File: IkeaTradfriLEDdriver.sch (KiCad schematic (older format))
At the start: 17 parts, among them J2 IKEA Zigbit module, J3 led strip, Q1 BUZ11, Q2 BC547, U1 LM741, U2 LM1117-3.3

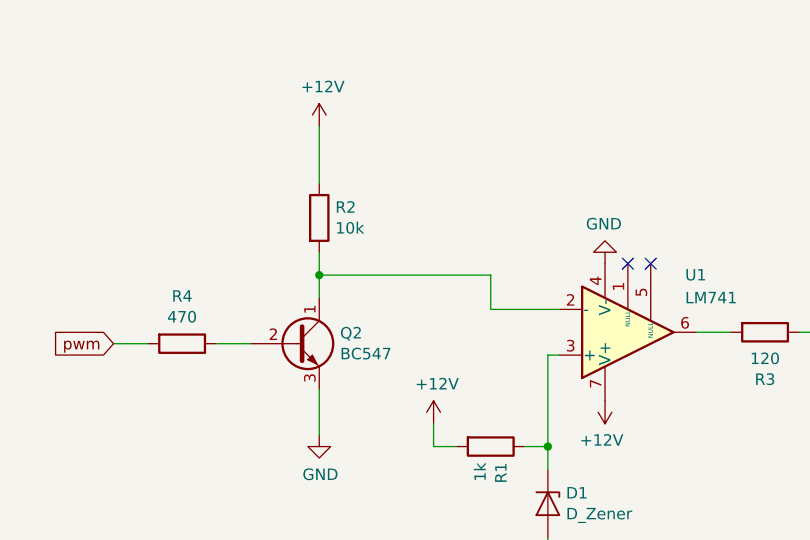
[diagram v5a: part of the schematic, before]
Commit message: Chybejici rezistor, opravene schema
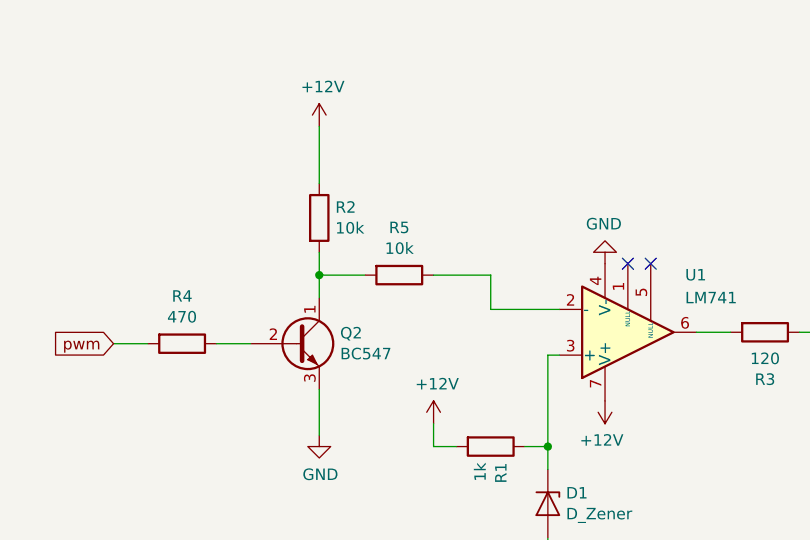
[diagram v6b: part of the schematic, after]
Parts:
- added R5: 10k, symbol Device:R
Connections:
- net at Q2.1 (C), R2.2: now also R5.2; no longer U1.2 (-)
- new net: R5.1, U1.2 (-)
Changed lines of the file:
@@
 	3250 3450 3250 3250
-Wire Wire Line
-	3250 2850 3250 2750
 Wire Wire Line
 	3250 2350 3250 2100
 Wire Wire Line
-	3250 2750 4000 2750
-Wire Wire Line
 	4000 2750 4000 2900
-Connection ~ 3250 2750
-Wire Wire Line
-	3250 2750 3250 2650
 $Comp
 L Connector:Conn_01x04_Male J3
@@
 Wire Wire Line
 	1250 2600 1250 2900
+Wire Wire Line
+	3250 2650 3250 2750
+$Comp
+L Device:R R5
+U 1 1 5C76BFEA
+P 3600 2750
+F 0 "R5" V 3393 2750 50  0000 C CNN
+F 1 "10k" V 3484 2750 50  0000 C CNN
+F 2 "" V 3530 2750 50  0001 C CNN
+F 3 "~" H 3600 2750 50  0001 C CNN
+	1    3600 2750
+	0    1    1    0
+$EndComp
+Wire Wire Line
+	3750 2750 4000 2750
+Wire Wire Line
+	3450 2750 3250 2750
+Connection ~ 3250 2750
+Wire Wire Line
+	3250 2750 3250 2850
 $EndSCHEMATC

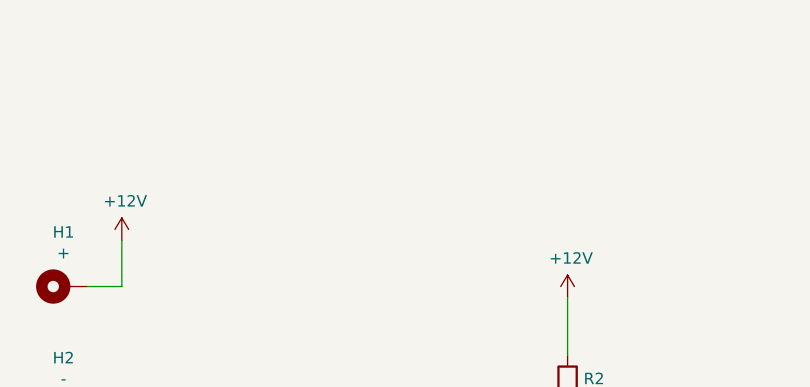
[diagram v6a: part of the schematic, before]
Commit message: Nejake divoke a nepovedene upravy
Stahoval jsem aktualizaci 3d modelu, ale do slozky se neda zapsat, takze 6 hodin cekani a smula :(
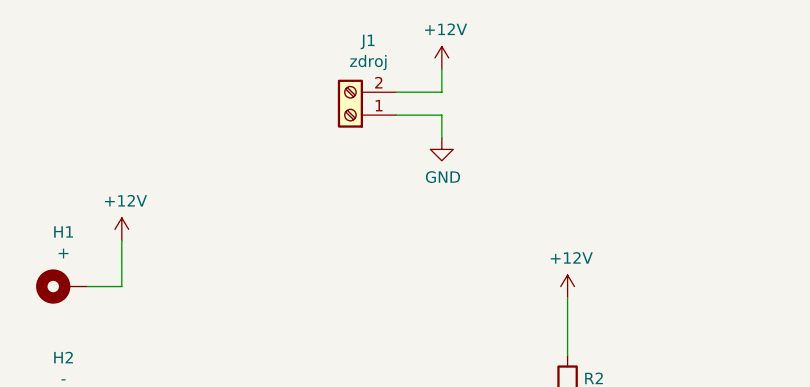
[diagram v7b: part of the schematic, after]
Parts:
- added J1: zdroj, TerminalBlock:TerminalBlock_Altech_AK300-2_P5.00mm, symbol Connector:Screw_Terminal_01x02
- R5: footprint (none) -> Resistor_THT:R_Axial_DIN0207_L6.3mm_D2.5mm_P7.62mm_Horizontal
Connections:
- net +12V: now also J1.2 (Pin_2)
- net GND: now also J1.1 (Pin_1)
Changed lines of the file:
@@
 F 0 "R5" V 3393 2750 50  0000 C CNN
 F 1 "10k" V 3484 2750 50  0000 C CNN
-F 2 "" V 3530 2750 50  0001 C CNN
+F 2 "Resistor_THT:R_Axial_DIN0207_L6.3mm_D2.5mm_P7.62mm_Horizontal" V 3530 2750 50  0001 C CNN
 F 3 "~" H 3600 2750 50  0001 C CNN
 	1    3600 2750
@@
 Wire Wire Line
 	3250 2750 3250 2850
+$Comp
+L Connector:Screw_Terminal_01x02 J1
+U 1 1 5C77C779
+P 2300 1300
+F 0 "J1" H 2220 975 50  0000 C CNN
+F 1 "zdroj" H 2220 1066 50  0000 C CNN
+F 2 "TerminalBlock:TerminalBlock_Altech_AK300-2_P5.00mm" H 2300 1300 50  0001 C CNN
+F 3 "~" H 2300 1300 50  0001 C CNN
+	1    2300 1300
+	-1   0    0    1
+$EndComp
+$Comp
+L power:+12V #PWR02
+U 1 1 5C77C89D
+P 2700 1100
+F 0 "#PWR02" H 2700 950 50  0001 C CNN
+F 1 "+12V" H 2715 1273 50  0000 C CNN
+F 2 "" H 2700 1100 50  0001 C CNN
+F 3 "" H 2700 1100 50  0001 C CNN
+	1    2700 1100
+	1    0    0    -1
+$EndComp
+$Comp
+L power:GND #PWR03
+U 1 1 5C77C8F3
+P 2700 1400
+F 0 "#PWR03" H 2700 1150 50  0001 C CNN
+F 1 "GND" H 2705 1227 50  0000 C CNN
+F 2 "" H 2700 1400 50  0001 C CNN
+F 3 "" H 2700 1400 50  0001 C CNN
+	1    2700 1400
+	1    0    0    -1
+$EndComp
+Wire Wire Line
+	2500 1200 2700 1200
+Wire Wire Line
+	2700 1200 2700 1100
+Wire Wire Line
+	2500 1300 2700 1300
+Wire Wire Line
+	2700 1300 2700 1400
 $EndSCHEMATC

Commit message: Nova deska + gerber soubory
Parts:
- removed D1: D_Zener, Diode_THT:D_A-405_P12.70mm_Horizontal, symbol Device:D_Zener
- removed H1: +, MountingHole:MountingHole_2.5mm_Pad, symbol Mechanical:MountingHole_Pad
- removed H2: -, MountingHole:MountingHole_2.5mm_Pad, symbol Mechanical:MountingHole_Pad
- removed Q2: BC547, Package_TO_SOT_THT:TO-92_Inline, symbol Transistor_BJT:BC547
- removed R2: 10k, Resistor_THT:R_Axial_DIN0309_L9.0mm_D3.2mm_P12.70mm_Horizontal, symbol Device:R
- removed R5: 10k, Resistor_THT:R_Axial_DIN0207_L6.3mm_D2.5mm_P7.62mm_Horizontal, symbol Device:R
- added D1: 1N4148, Diode_THT:D_DO-35_SOD27_P7.62mm_Horizontal, symbol Diode:1N4148
- R3: value 120 -> 220
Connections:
- net +12V: now also J3.1 (Pin_1), J3.2 (Pin_2), J3.3 (Pin_3), R1.1; no longer R1.2
- net GND: now also D1.1 (K); no longer J3.4 (Pin_4)
- net at U1.3 (+): now also R4.1; no longer R1.1
- net at U1.2 (-): now also R1.2, D1.2 (A)
- new net: J3.4 (Pin_4), Q1.2 (D)
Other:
- note added: "pwm je v urovni 3.3V\n"
- moved on the sheet: J1, J3, Q1, R1, R3, R4, U1
